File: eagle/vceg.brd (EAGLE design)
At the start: 100 x 80 mm, 58 parts, among them IC1 4052N, IC2 4001N, IC3 TL074P, IC4 CA3080E, Q1 2N3906INLINE, Q2 2N3906INLINE, U1 POWER

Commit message: down to one flyer
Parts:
- moved TG_SWA_1 55.1 mm to (92.7, 24.1)
- moved R21 41.5 mm to (88.9, 29.2), turned to 270 degrees
- moved LFO_SW_1 35.1 mm to (78.7, 71.1)
- moved C2 29.5 mm to (72.4, 71.1)
- moved R25 19.3 mm to (72.4, 62.2), turned to 0 degrees
- moved GATE 18.2 mm to (67.3, 71.1)
- moved R5 17.8 mm to (55.9, 62.2), turned to 0 degrees
- moved R19 17.1 mm to (74.9, 20.3), turned to 180 degrees
- moved ATTACK 15.7 mm to (7.62, 20.3)
- moved R20 14.9 mm to (67.3, 67.3), turned to 180 degrees
- moved R29 14.0 mm to (41.9, 50.8)
- moved R16 14.0 mm to (36.8, 50.8)
- moved IC4 13.1 mm to (52.1, 47.0)
- moved TG_SWB_1 8.98 mm to (38.1, 43.2)
- moved IC2 8.98 mm to (91.4, 48.3)
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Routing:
- net GND: track 0.00 -> 442.3 mm
- net +12V: track 0.00 -> 370.3 mm
- net N$11: track 0.00 -> 112.9 mm
- net N$31: track 0.00 -> 102.3 mm
- net N$2: track 0.00 -> 61.1 mm
- net N$28: track 0.00 -> 54.9 mm
- net N$14: track 0.00 -> 51.8 mm
- net N$34: track 0.00 -> 49.0 mm
- net N$5: track 0.00 -> 37.2 mm
- net N$24: track 0.00 -> 33.1 mm
- net N$21: track 0.00 -> 32.8 mm
- net N$20: track 0.00 -> 32.2 mm
- net N$26: track 0.00 -> 31.1 mm
- net N$17: track 0.00 -> 29.8 mm
- net N$25: track 0.00 -> 26.8 mm
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
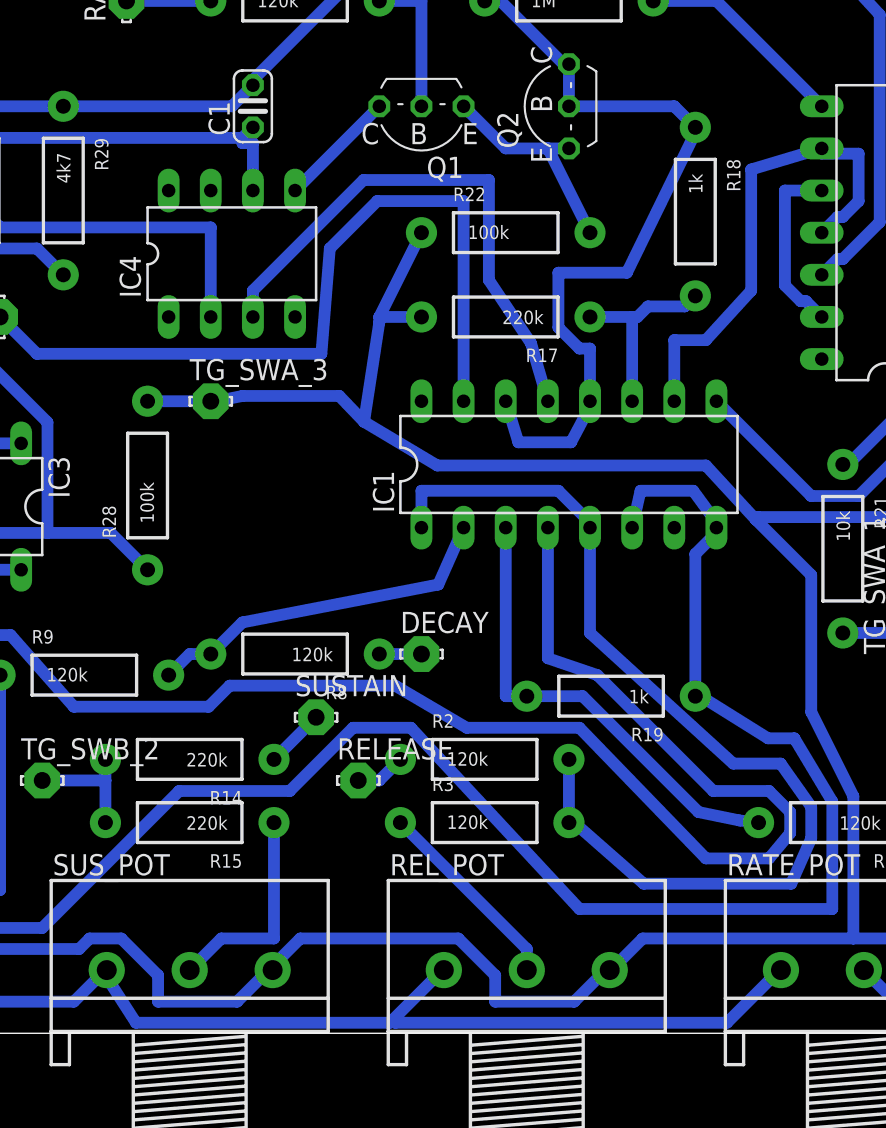
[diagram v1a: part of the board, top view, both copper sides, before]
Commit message: remembered to power tl074
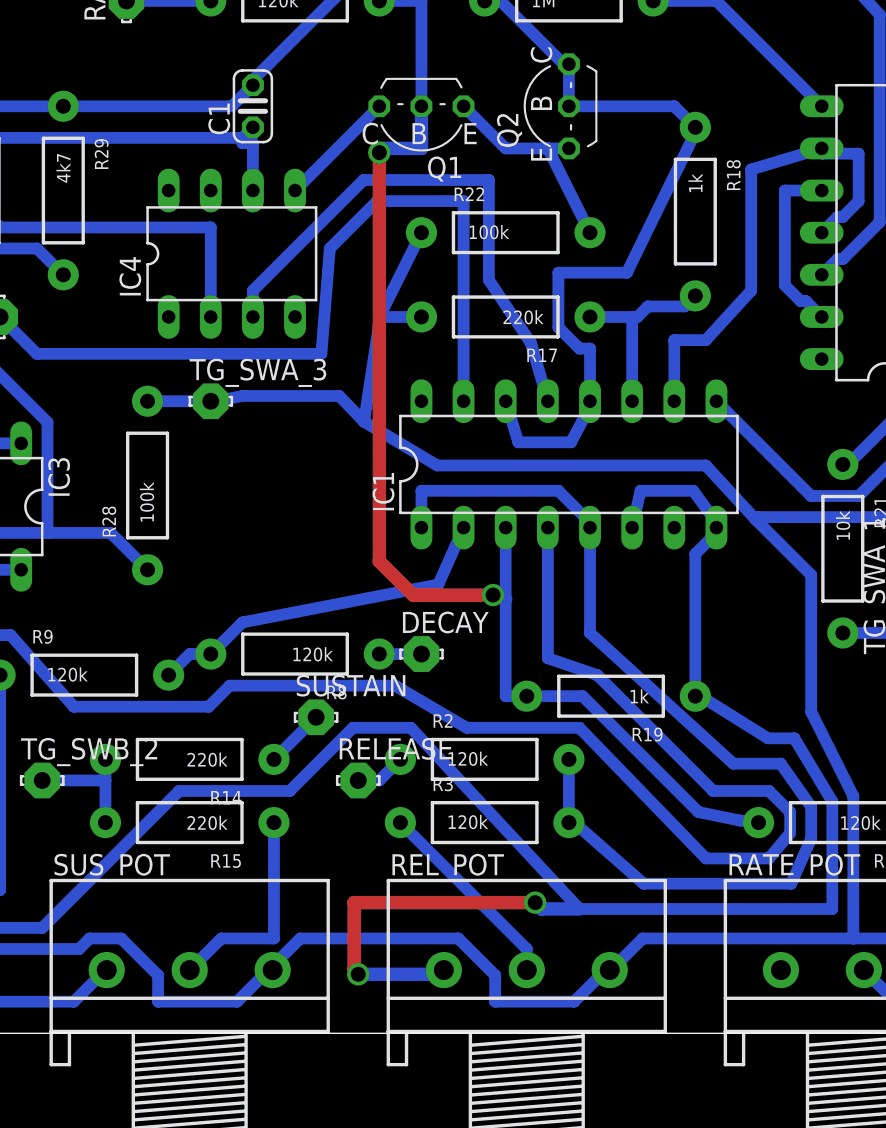
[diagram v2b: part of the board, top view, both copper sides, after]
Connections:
- removed net V+: IC3.4
- removed net V-: IC3.11
- net +12V: now also IC3.4
- net -12V: now also IC3.11
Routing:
- net N$5: track 37.2 -> 75.6 mm, vias 0 -> 2
- net GND: track 442.3 -> 417.3 mm, vias 0 -> 2
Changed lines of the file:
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@@
 <wire x1="44.45" y1="3.81" x2="44.53" y2="3.81" width="0.7112" layer="16"/>
 <wire x1="24.4475" y1="3.81" x2="24.21" y2="3.81" width="0.7112" layer="16"/>
-<wire x1="61.595" y1="0.635" x2="61.75375" y2="0.79375" width="0.7112" layer="16"/>
-<wire x1="61.75375" y1="0.79375" x2="64.77" y2="3.81" width="0.7112" layer="16"/>
-<wire x1="46.2915" y1="0.635" x2="61.595" y2="0.635" width="0.7112" layer="16"/>
-<wire x1="44.45" y1="3.4925" x2="46.2915" y2="0.635" width="0.7112" layer="16"/>
-<wire x1="64.77" y1="3.81" x2="64.85" y2="3.81" width="0.7112" layer="16"/>
-<wire x1="44.45" y1="3.4925" x2="44.53" y2="3.81" width="0.7112" layer="16"/>
-<wire x1="81.915" y1="0.635" x2="85.09" y2="3.81" width="0.7112" layer="16"/>
-<wire x1="61.9125" y1="0.635" x2="81.915" y2="0.635" width="0.7112" layer="16"/>
-<wire x1="85.09" y1="3.81" x2="85.17" y2="3.81" width="0.7112" layer="16"/>
-<wire x1="61.9125" y1="0.635" x2="61.75375" y2="0.79375" width="0.7112" layer="16"/>
 <wire x1="84.3915" y1="17.78" x2="80.3275" y2="20.32" width="0.7112" layer="16"/>
 <wire x1="85.979" y1="17.78" x2="84.3915" y2="17.78" width="0.7112" layer="16"/>
@@
 <wire x1="17.145" y1="18.7325" x2="13.335" y2="18.7325" width="0.7112" layer="16"/>
 <wire x1="17.145" y1="18.7325" x2="17.145" y2="18.415" width="0.7112" layer="16"/>
+<wire x1="88.265" y1="7.493" x2="85.17" y2="3.81" width="0" layer="19" extent="16-16"/>
+<wire x1="73.025" y1="7.493" x2="70.739" y2="7.493" width="0.8128" layer="16"/>
+<wire x1="70.739" y1="7.493" x2="70.358" y2="7.874" width="0.8128" layer="16"/>
+<via x="70.358" y="7.874" extent="1-16" drill="0.9" shape="square"/>
+<wire x1="70.358" y1="7.874" x2="59.436" y2="7.874" width="0.8128" layer="1"/>
+<wire x1="59.436" y1="7.874" x2="59.436" y2="3.81" width="0.8128" layer="1"/>
+<wire x1="59.436" y1="3.81" x2="59.69" y2="3.556" width="0.8128" layer="1"/>
+<via x="59.69" y="3.556" extent="1-16" drill="0.9" shape="square"/>
+<wire x1="59.69" y1="3.556" x2="64.596" y2="3.556" width="0.8128" layer="16"/>
+<wire x1="64.596" y1="3.556" x2="64.85" y2="3.81" width="0.8128" layer="16"/>
 </signal>
 <signal name="VCC">
@@
 <signal name="VDD">
 <contactref element="IC2" pad="14"/>
-</signal>
-<signal name="V+">
-<contactref element="IC3" pad="4"/>
-</signal>
-<signal name="V-">
-<contactref element="IC3" pad="11"/>
 </signal>
 <signal name="+12V">
@@
 <wire x1="83.82" y1="31.115" x2="98.7425" y2="31.115" width="0.7112" layer="16"/>
 <wire x1="83.82" y1="31.115" x2="83.66125" y2="30.95625" width="0.7112" layer="16"/>
+<contactref element="IC3" pad="4"/>
+<wire x1="46.99" y1="38.1" x2="31.75" y2="35.56" width="0" layer="19" extent="1-1"/>
 </signal>
 <signal name="-12V">
@@
 <contactref element="U1" pad="2"/>
 <wire x1="15.24" y1="72.39" x2="15.24" y2="69.85" width="0.7112" layer="16"/>
+<contactref element="IC3" pad="11"/>
+<wire x1="31.75" y1="27.94" x2="15.24" y2="69.85" width="0" layer="19" extent="1-1"/>
 </signal>
 <signal name="N$4">
@@
 <contactref element="R19" pad="P$2"/>
 <contactref element="Q1" pad="B"/>
-<wire x1="68.58" y1="20.32" x2="68.58" y2="30.48" width="0.7112" layer="16"/>
+<wire x1="68.58" y1="20.32" x2="68.58" y2="26.162" width="0.7112" layer="16"/>
+<wire x1="68.58" y1="26.162" x2="68.58" y2="30.48" width="0.7112" layer="16"/>
 <wire x1="69.85" y1="20.32" x2="68.58" y2="20.32" width="0.7112" layer="16"/>
 <wire x1="82.677" y1="12.827" x2="83.82" y2="12.7" width="0.7112" layer="16"/>
@@
 <wire x1="63.5" y1="62.23" x2="63.5" y2="55.88" width="0.7112" layer="16"/>
 <wire x1="60.96" y1="62.23" x2="63.5" y2="62.23" width="0.7112" layer="16"/>
-<wire x1="68.58" y1="30.48" x2="63.5" y2="55.88" width="0" layer="19" extent="1-1"/>
+<wire x1="63.5" y1="55.88" x2="63.5" y2="53.34" width="0.8128" layer="16"/>
+<wire x1="63.5" y1="53.34" x2="61.214" y2="53.34" width="0.8128" layer="16"/>
+<wire x1="61.214" y1="53.34" x2="60.96" y2="53.086" width="0.8128" layer="16"/>
+<via x="60.96" y="53.086" extent="1-16" drill="0.9" shape="square"/>
+<wire x1="60.96" y1="53.086" x2="60.96" y2="28.448" width="0.8128" layer="1"/>
+<wire x1="60.96" y1="28.448" x2="62.992" y2="26.416" width="0.8128" layer="1"/>
+<wire x1="62.992" y1="26.416" x2="67.818" y2="26.416" width="0.8128" layer="1"/>
+<via x="67.818" y="26.416" extent="1-16" drill="0.9" shape="square"/>
+<wire x1="67.818" y1="26.416" x2="68.326" y2="26.416" width="0.8128" layer="16"/>
+<wire x1="68.326" y1="26.416" x2="68.58" y2="26.162" width="0.8128" layer="16"/>
 </signal>
 <signal name="N$6">

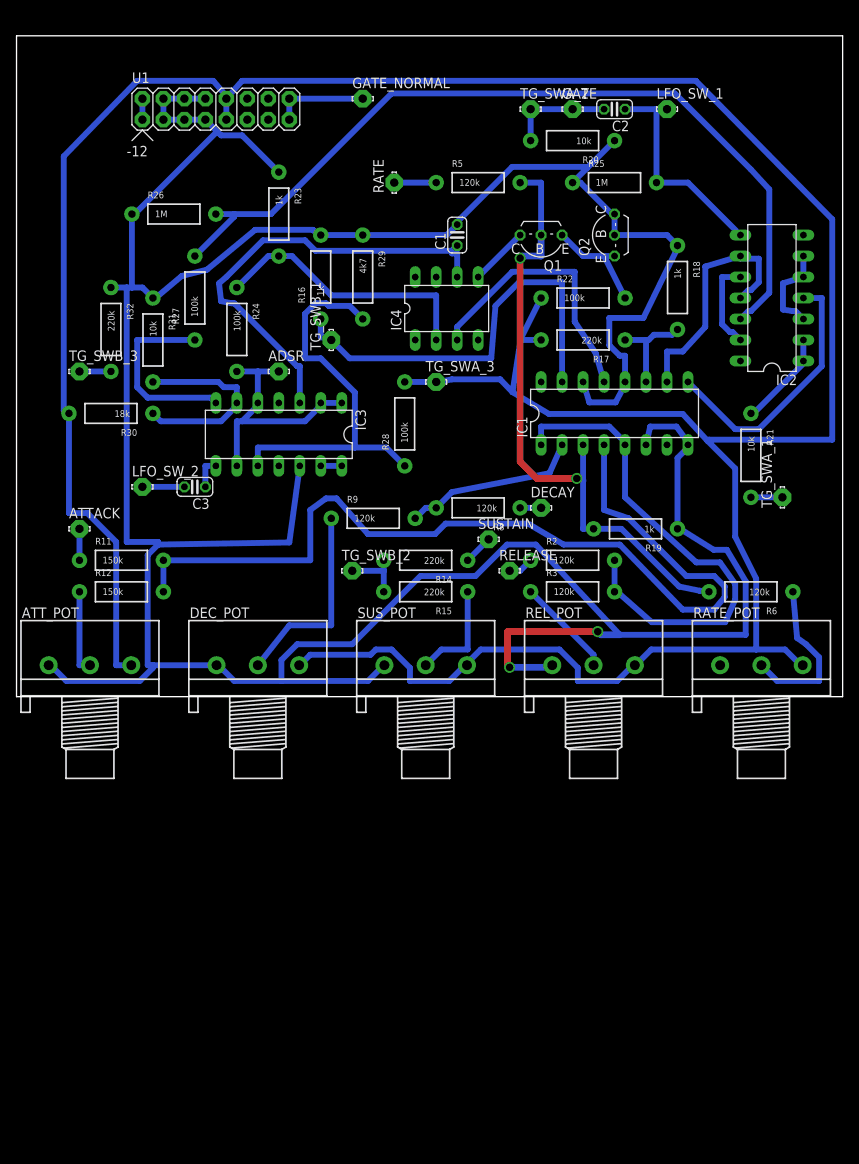
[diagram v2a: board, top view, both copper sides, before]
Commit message: ca3080 with power now
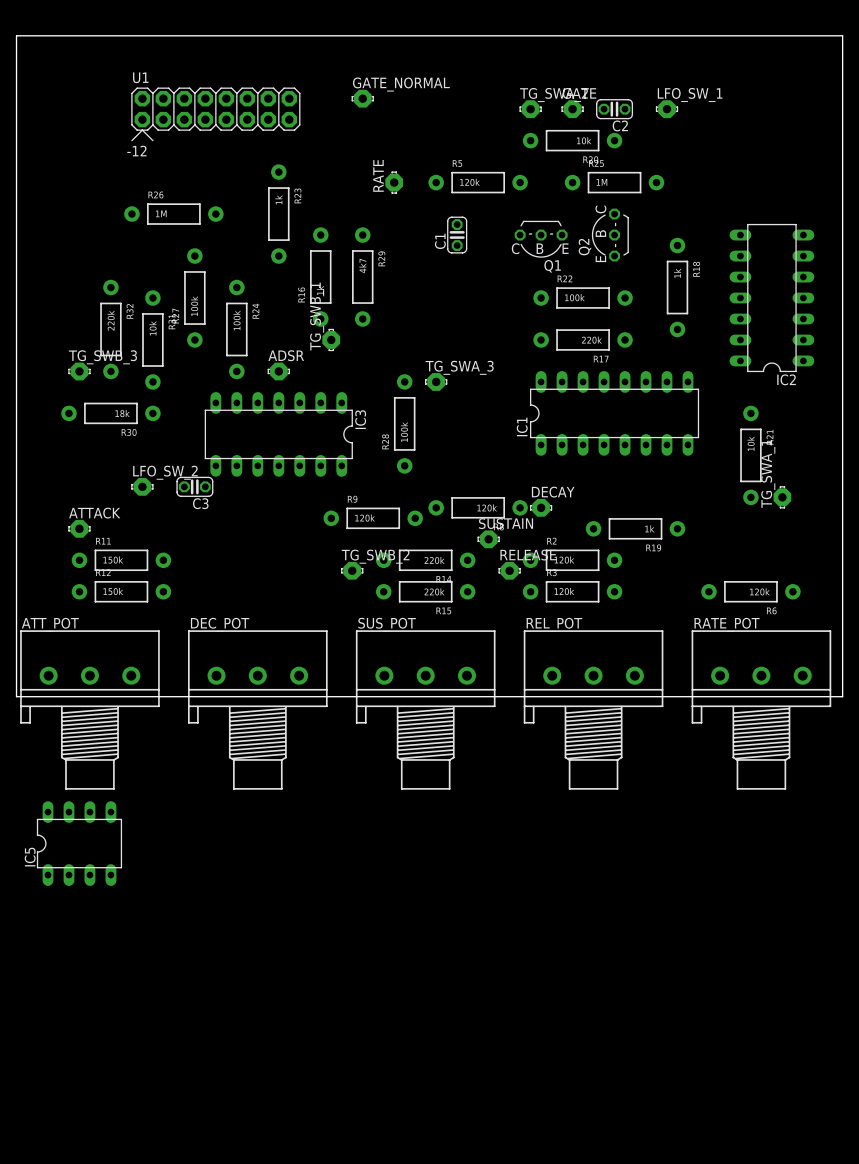
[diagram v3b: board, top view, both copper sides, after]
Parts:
- removed IC4: CA3080E, synthdiy:DIL08
- added IC5: CA3080E, ota:DIL08
- moved ATT_POT 1.27 mm to (8.89, 2.54)
- moved DEC_POT 1.27 mm to (29.2, 2.54)
- moved RATE_POT 1.27 mm to (90.2, 2.54)
- moved REL_POT 1.27 mm to (69.8, 2.54)
- moved SUS_POT 1.27 mm to (49.5, 2.54)
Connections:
- removed net N$23: IC4.5, Q1.C
- new net N$41: IC1.13, IC5.3
- net +12V: now also IC5.7
- net -12V: now also IC5.4
- net N$21: now also IC5.5, Q1.C; no longer IC1.13, IC4.3
- net N$24: now also IC5.2; no longer IC4.2
- net N$28: now also IC5.6; no longer IC4.6
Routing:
- net GND: track 417.3 -> 0.00 mm, vias 2 -> 0
- net +12V: track 370.3 -> 0.00 mm
- net N$11: track 112.9 -> 0.00 mm
- net N$31: track 102.3 -> 0.00 mm
- net N$5: track 75.6 -> 0.00 mm, vias 2 -> 0
- net N$2: track 61.1 -> 0.00 mm
- net N$28: track 54.9 -> 0.00 mm
- net N$14: track 51.8 -> 0.00 mm
- net N$34: track 49.0 -> 0.00 mm
- net N$24: track 33.1 -> 0.00 mm
- net N$21: track 32.8 -> 0.00 mm
- net N$20: track 32.2 -> 0.00 mm
- net N$26: track 31.1 -> 0.00 mm
- net N$17: track 29.8 -> 0.00 mm
- net N$25: track 26.8 -> 0.00 mm
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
